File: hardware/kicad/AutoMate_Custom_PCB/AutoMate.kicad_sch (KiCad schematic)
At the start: 74 parts, among them J1 8P8C, J11_Doorsensor1 Conn_01x02_Socket, J12_ZMCT103C1 Conn_01x02_Socket, J2_BH1750 Conn_01x05_Socket, J2_IR_AHT_BH17 Conn_01x05_Socket, J2_IR_AHT_BH18 Conn_01x05_Socket, J2_PCA9685_Female1 PCA9685, J2_PCA9685_Male1 PCA9685, J5_Relay1 Relay, J9_AHT_BMP1 Conn_01x04_Socket, J9_ZMPT1 Conn_01x04_Socket, SW1_Manual_Override1 SW_DIP_x12, T1 Screw_Terminal_01x02, T10 ST01x02, T11 ST01x02, T12 ST01x02, T13 ST01x02, T14 ST01x02, T15 ST01x02, T2 Screw_Terminal_01x02, T3 Screw_Terminal_01x02, T4 Screw_Terminal_01x02, T5 Screw_Terminal_01x02, T6 Screw_Terminal_01x02, T7 Screw_Terminal_01x02, T8 ST01x02, T9 ST01x02, U1 815, U1_ESP32-DEVKITC1 ESP32-DEVKITC, U2_74HC595 74HC595

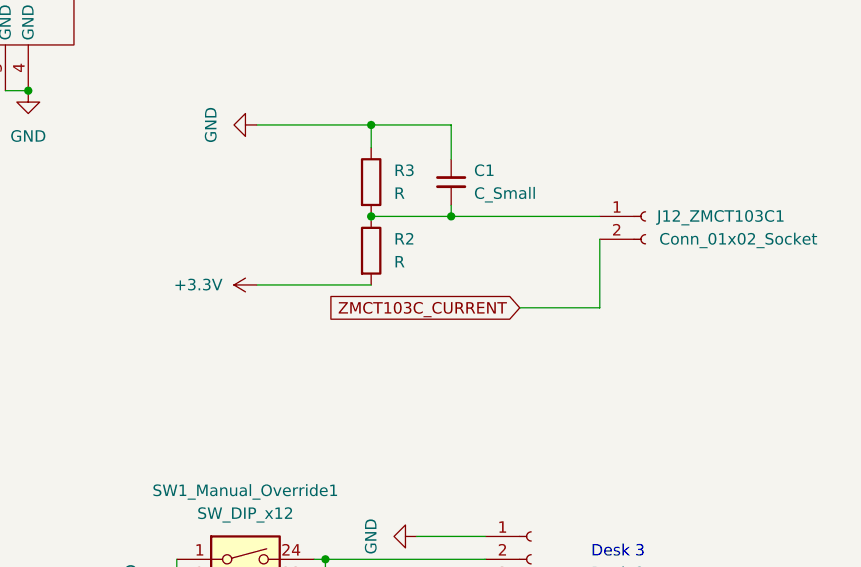
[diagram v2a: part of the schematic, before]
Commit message: deploy: v1.0.6 - Fixed state restoration race condition on boot
- Added boot_complete global flag to prevent binary sensor automations from running during boot
- Rewrote on_boot lambda to restore lights first, then relays atomically
- Updated non_ceiling_pwm_active, ceiling_pwm_active, desks_active binary sensors to check boot_complete before controlling relays
- This prevents the race condition where binary sensor on_state handlers would turn off relays after they were restored
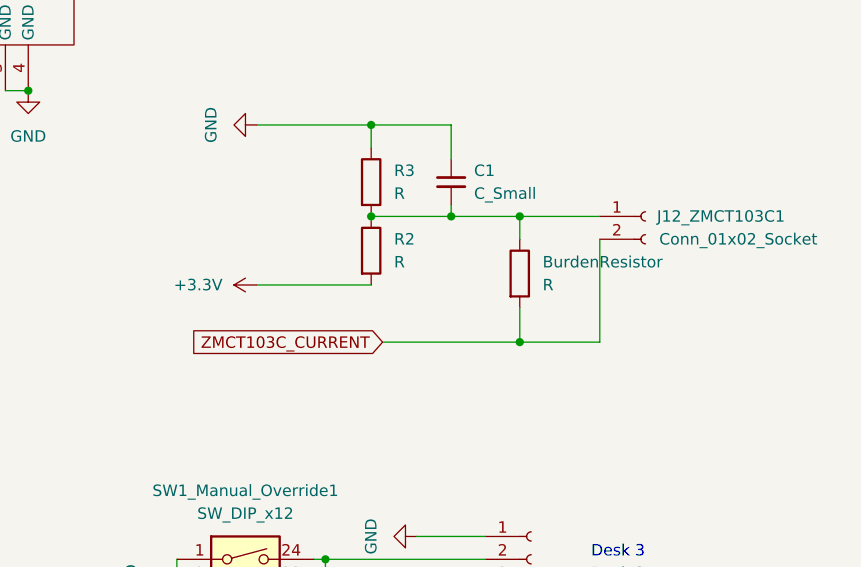
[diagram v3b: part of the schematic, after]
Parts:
- added BurdenResistor: R, Resistor_THT:R_Axial_DIN0411_L9.9mm_D3.6mm_P5.08mm_Vertical, symbol Device:R
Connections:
- net ZMCT103C_CURRENT: now also BurdenResistor.2
- net at C1.2, J12_ZMCT103C1.1 (Pin_1), R2.1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: now also BurdenResistor.1
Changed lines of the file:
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@@
 	)
 	(junction
+		(at 184.15 194.31)
+		(diameter 0)
+		(color 0 0 0 0)
+	)
+	(junction
 		(at 86.36 100.33)
 		(diameter 0)
@@
 	)
 	(junction
+		(at 184.15 208.28)
+		(diameter 0)
+		(color 0 0 0 0)
+	)
+	(junction
 		(at 109.22 180.34)
 		(diameter 0)
@@
 	(wire
 		(pts
+			(xy 184.15 208.28) (xy 193.04 208.28)
+		)
+		(stroke
+			(width 0)
+			(type default)
+		)
+	)
+	(wire
+		(pts
 			(xy 161.29 274.32) (xy 161.29 275.59)
 		)
@@
 	(wire
 		(pts
-			(xy 184.15 204.47) (xy 193.04 204.47)
+			(xy 168.91 208.28) (xy 184.15 208.28)
 		)
 		(stroke
@@
 	(wire
 		(pts
-			(xy 176.53 194.31) (xy 193.04 194.31)
+			(xy 176.53 194.31) (xy 184.15 194.31)
+		)
+		(stroke
+			(width 0)
+			(type default)
+		)
+	)
+	(wire
+		(pts
+			(xy 184.15 204.47) (xy 184.15 208.28)
 		)
 		(stroke
@@
 	(wire
 		(pts
+			(xy 184.15 194.31) (xy 193.04 194.31)
+		)
+		(stroke
+			(width 0)
+			(type default)
+		)
+	)
+	(wire
+		(pts
 			(xy 154.94 184.15) (xy 167.64 184.15)
 		)
@@
 	(wire
 		(pts
+			(xy 184.15 194.31) (xy 184.15 196.85)
+		)
+		(stroke
+			(width 0)
+			(type default)
+		)
+	)
+	(wire
+		(pts
 			(xy 146.05 257.81) (xy 146.05 260.35)
 		)
@@
 	(wire
 		(pts
-			(xy 193.04 204.47) (xy 193.04 196.85)
+			(xy 193.04 208.28) (xy 193.04 196.85)
 		)
 		(stroke
@@
 	(global_label "ZMCT103C_CURRENT"
 		(shape input)
-		(at 184.15 204.47 180)
+		(at 168.91 208.28 180)
 		(fields_autoplaced yes)
 		(effects
@@
 		)
 		(property "Intersheetrefs" "${INTERSHEET_REFS}"
-			(at 161.8126 204.47 0)
+			(at 146.5726 208.28 0)
 			(hide yes)
 			(show_name no)
@@
 					(unit 1)
 				)
+			)
+		)
+	)
+	(symbol
+		(lib_id "Device:R")
+		(at 184.15 200.66 0)
+		(unit 1)
+		(body_style 1)
+		(exclude_from_sim no)
+		(in_bom yes)
+		(on_board yes)
+		(in_pos_files yes)
+		(dnp no)
+		(fields_autoplaced yes)
+		(property "Reference" "BurdenResistor"
+			(at 186.69 199.3899 0)
+			(show_name no)
+			(do_not_autoplace no)
+			(effects
+				(font
+					(size 1.27 1.27)
+				)
+				(justify left)
+			)
+		)
+		(property "Value" "R"
+			(at 186.69 201.9299 0)
+			(show_name no)
+			(do_not_autoplace no)
+			(effects
+				(font
+					(size 1.27 1.27)
+				)
+				(justify left)
+			)
+		)
+		(property "Footprint" "Resistor_THT:R_Axial_DIN0411_L9.9mm_D3.6mm_P5.08mm_Vertical"
+			(at 182.372 200.66 90)
+			(hide yes)
+			(show_name no)
+			(do_not_autoplace no)
+			(effects
+				(font
+					(size 1.27 1.27)
+				)
+			)
+		)
+		(property "Datasheet" ""
+			(at 184.15 200.66 0)
+			(hide yes)
+			(show_name no)
+			(do_not_autoplace no)
+			(effects
+				(font
+					(size 1.27 1.27)
+				)
+			)
+		)
+		(property "Description" "Resistor"
+			(at 184.15 200.66 0)
+			(hide yes)
+			(show_name no)
+			(do_not_autoplace no)
+			(effects
+				(font
+					(size 1.27 1.27)
+				)
+			)
+		)
+		(pin "2"
+		)
+		(pin "1"
+		)
+		(instances
+			(project "AutoMate"
+				(path "/6e78f634-a06d-4f9f-a273-756e182159e5"
+					(reference "BurdenResistor")
+					(unit 1)
+				)
